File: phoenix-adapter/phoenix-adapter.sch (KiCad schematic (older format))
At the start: 1 part, among them CON101 RCJ-2223

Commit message: First commit, replaced with JST XH connector
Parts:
- CON101: footprint db-thparts:RCJ-2223 -> Connector_JST:JST_XH_S03B-XH-A_1x03_P2.50mm_Horizontal; symbol RCJ-2223 -> Connector:Conn_01x03_Male; Description CONN RCA JACK MONO 3.2MM R/A -> CONN JST XH 3-Pin Side; Digikey CP-1435-ND -> (none)
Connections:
- wire segments 3 -> 4
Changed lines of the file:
@@
-EESchema Schematic File Version 2
-LIBS:power
-LIBS:db-connectors
-LIBS:db-diodes
-LIBS:db-mcu
-LIBS:db-memory
-LIBS:db-passives
-LIBS:db-sem
-LIBS:db-transistors
-LIBS:db-vgparts
+EESchema Schematic File Version 4
 LIBS:phoenix-adapter-cache
-EELAYER 25 0
+EELAYER 26 0
 EELAYER END
 $Descr A4 11693 8268
@@
 $EndBitmap
 $Comp
-L RCJ-2223 CON101
+L Connector:Conn_01x03_Male CON101
 U 1 1 5ABE576C
-P 5250 2950
-F 0 "CON101" H 5350 3025 50  0000 C CNN
-F 1 "RCJ-2223" H 5450 3100 50  0000 C CNN
-F 2 "db-thparts:RCJ-2223" H 5775 3525 60  0001 C CNN
-F 3 "https://www.cui.com/product/resource/rcj-22xx.pdf" H 6475 3225 60  0001 C CNN
-F 4 "CP-1435-ND" H 5575 3325 60  0001 C CNN "Digikey"
-F 5 "CONN RCA JACK MONO 3.2MM R/A" H 6050 3425 60  0001 C CNN "Description"
-	1    5250 2950
+P 5050 3100
+F 0 "CON101" H 5150 3175 50  0000 C CNN
+F 1 "RCJ-2223" H 5250 3250 50  0000 C CNN
+F 2 "Connector_JST:JST_XH_S03B-XH-A_1x03_P2.50mm_Horizontal" H 5575 3675 60  0001 C CNN
+F 3 "" H 6275 3375 60  0001 C CNN
+F 4 "CONN JST XH 3-Pin Side" H 5850 3575 60  0001 C CNN "Description"
+	1    5050 3100
 	1    0    0    -1
 $EndComp
 $Comp
-L GND #PWR?
+L power:GND #PWR0101
 U 1 1 5ABE5F05
-P 5250 3450
-F 0 "#PWR?" H 5250 3200 50  0001 C CNN
-F 1 "GND" H 5250 3300 50  0000 C CNN
-F 2 "" H 5250 3450 50  0001 C CNN
-F 3 "" H 5250 3450 50  0001 C CNN
-	1    5250 3450
+P 6030 3265
+F 0 "#PWR0101" H 6030 3015 50  0001 C CNN
+F 1 "GND" H 6030 3115 50  0000 C CNN
+F 2 "" H 6030 3265 50  0001 C CNN
+F 3 "" H 6030 3265 50  0001 C CNN
+	1    6030 3265
 	1    0    0    -1
 $EndComp
+Text Label 5650 3200 0    60   ~ 0
+LEFT
+Text Label 5650 3000 0    60   ~ 0
+RIGHT
 Wire Wire Line
-	5600 3175 5950 3175
+	6030 3100 6030 3265
 Wire Wire Line
-	5600 3025 5950 3025
+	5250 3100 6030 3100
 Wire Wire Line
-	5250 3325 5250 3450
-Text Label 5650 3175 0    60   ~ 0
-LEFT
-Text Label 5650 3025 0    60   ~ 0
-RIGHT
+	5250 3200 5950 3200
+Wire Wire Line
+	5250 3000 5950 3000
 $EndSCHEMATC

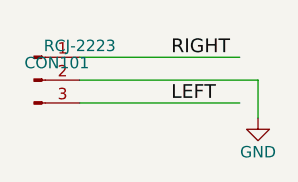
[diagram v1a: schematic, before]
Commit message: Add back Rene's logo to the PCB, relabel some things on schematic
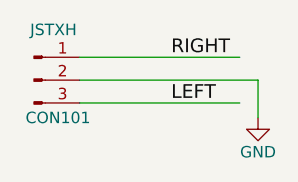
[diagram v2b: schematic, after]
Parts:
- CON101: value RCJ-2223 -> JSTXH
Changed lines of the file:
@@
 U 1 1 5ABE576C
 P 5050 3100
-F 0 "CON101" H 5150 3175 50  0000 C CNN
-F 1 "RCJ-2223" H 5250 3250 50  0000 C CNN
+F 0 "CON101" H 5155 2935 50  0000 C CNN
+F 1 "JSTXH" H 5135 3320 50  0000 C CNN
 F 2 "Connector_JST:JST_XH_S03B-XH-A_1x03_P2.50mm_Horizontal" H 5575 3675 60  0001 C CNN
 F 3 "" H 6275 3375 60  0001 C CNN
